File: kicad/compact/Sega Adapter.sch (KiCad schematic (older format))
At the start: 5 parts, among them J1 Sega, J2 Atari, U1 PIC16F1847

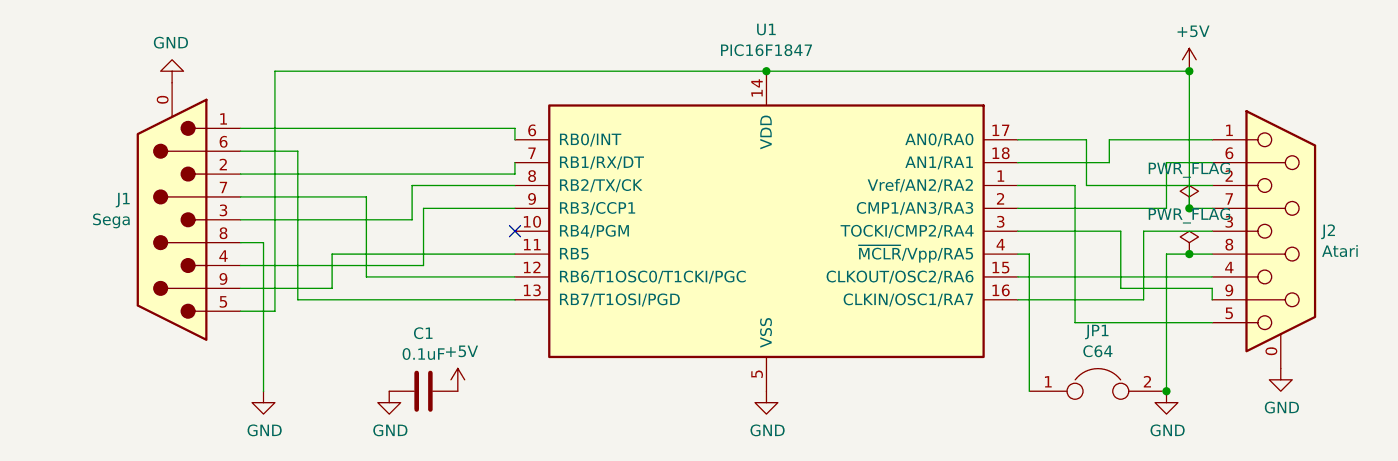
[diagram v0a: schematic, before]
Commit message: Switch compact adapter to IDC connector
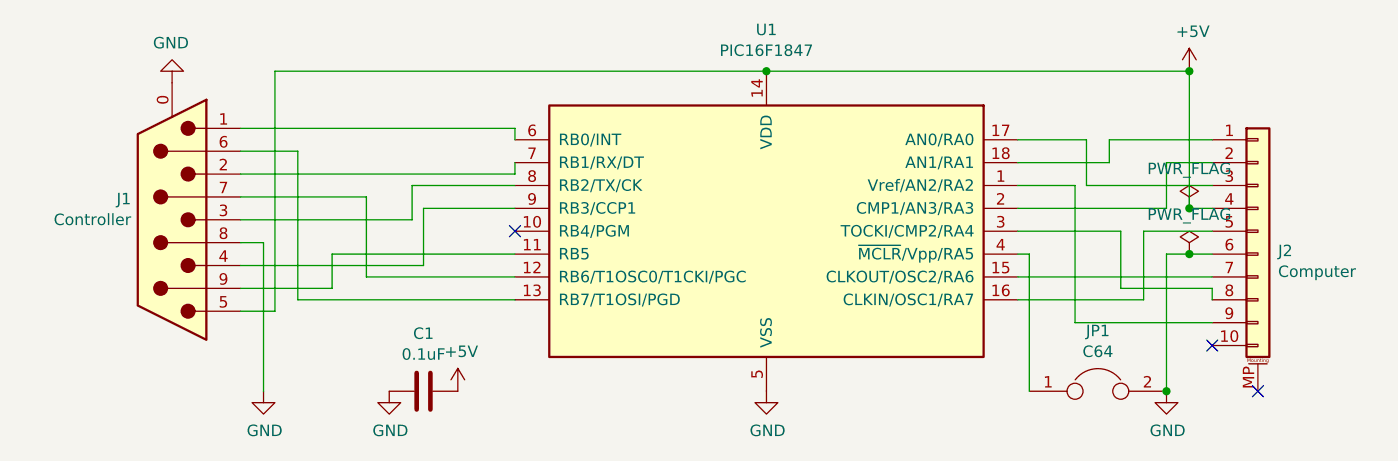
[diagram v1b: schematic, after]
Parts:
- removed J2: Atari, Connector_Dsub:DSUB-9_Female_Horizontal_P2.77x2.84mm_EdgePinOffset7.70mm_Housed_MountingHolesOffset9.12mm, symbol Connector:DB9_Female_MountingHoles
- added J2: Computer, Connector_PinHeader_2.54mm:PinHeader_2x05_P2.54mm_Vertical, symbol Connector_Generic_MountingPin:Conn_01x10_MountingPin
- J1: value Sega -> Controller
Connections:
- net +5V: now also J2.4 (Pin_4)
- net GND: now also J2.6 (Pin_6)
- net at U1.1 (Vref/AN2/RA2): now also J2.9 (Pin_9)
- net at U1.15 (CLKOUT/OSC2/RA6): now also J2.7 (Pin_7)
- net at U1.16 (CLKIN/OSC1/RA7): now also J2.5 (Pin_5)
- net at U1.17 (AN0/RA0): now also J2.3 (Pin_3)
- net at U1.18 (AN1/RA1): now also J2.1 (Pin_1)
- net at U1.2 (CMP1/AN3/RA3): now also J2.2 (Pin_2)
- net at U1.3 (TOCKI/CMP2/RA4): now also J2.8 (Pin_8)
- no-connect marks 1 -> 3
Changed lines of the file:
@@
 Sheet 1 1
 Title "Sega Adapter"
-Date "2021-03-15"
-Rev "2"
+Date "2021-07-06"
+Rev "3"
 Comp ""
 Comment1 ""
@@
 $EndComp
 $Comp
-L Connector:DB9_Female_MountingHoles J2
-U 1 1 601EC4D9
-P 9400 3950
-F 0 "J2" H 9580 3952 50  0000 L CNN
-F 1 "Atari" H 9580 3861 50  0000 L CNN
-F 2 "Connector_Dsub:DSUB-9_Female_Horizontal_P2.77x2.84mm_EdgePinOffset7.70mm_Housed_MountingHolesOffset9.12mm" H 9400 3950 50  0001 C CNN
-F 3 " ~" H 9400 3950 50  0001 C CNN
-	1    9400 3950
-	1    0    0    -1
-$EndComp
-$Comp
 L Connector:DB9_Male_MountingHoles J1
 U 1 1 601EDA30
 P 4550 3900
 F 0 "J1" H 4729 3809 50  0000 L CNN
-F 1 "Sega" H 4729 3900 50  0000 L CNN
+F 1 "Controller" H 4729 3900 50  0000 L CNN
 F 2 "Connector_Dsub:DSUB-9_Male_Horizontal_P2.77x2.84mm_EdgePinOffset7.70mm_Housed_MountingHolesOffset9.12mm" H 4550 3900 50  0001 C CNN
 F 3 " ~" H 4550 3900 50  0001 C CNN
@@
 $EndComp
 $Comp
-L power:GND #PWR0107
-U 1 1 6055DE77
-P 9400 4550
-F 0 "#PWR0107" H 9400 4300 50  0001 C CNN
-F 1 "GND" H 9405 4377 50  0000 C CNN
-F 2 "" H 9400 4550 50  0001 C CNN
-F 3 "" H 9400 4550 50  0001 C CNN
-	1    9400 4550
-	1    0    0    -1
-$EndComp
-$Comp
 L power:GND #PWR0108
 U 1 1 6055E6D2
@@
 	8900 4050 9000 4050
 Connection ~ 9000 4050
+$Comp
+L Connector_Generic_MountingPin:Conn_01x10_MountingPin J2
+U 1 1 60E5DF62
+P 9300 3950
+F 0 "J2" H 9388 3864 50  0000 L CNN
+F 1 "Computer" H 9388 3773 50  0000 L CNN
+F 2 "Connector_PinHeader_2.54mm:PinHeader_2x05_P2.54mm_Vertical" H 9300 3950 50  0001 C CNN
+F 3 "~" H 9300 3950 50  0001 C CNN
+	1    9300 3950
+	1    0    0    -1
+$EndComp
+NoConn ~ 9300 4650
+NoConn ~ 9100 4450
 $EndSCHEMATC
